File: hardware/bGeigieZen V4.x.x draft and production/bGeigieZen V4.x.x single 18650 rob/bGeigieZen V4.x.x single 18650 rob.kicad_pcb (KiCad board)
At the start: 2 copper layers, 129.4 x 64.6 mm, 13 parts, among them J1 M5 2x15 pin, J2 Geiger IRover, J3 GPS, J4 Geiger Safepulse, J5 Extra support header

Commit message: Added  Assembly manual and Japan Post registered mail numbers.
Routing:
- net /SCL: track 116.3 -> 117.7 mm
- net /GIO2 on Core and GIO32 on Core-2: track 90.4 -> 89.3 mm
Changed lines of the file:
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@@
 	(title_block
 		(title "bGeigieZen Draft V4.0.5 NFW")
-		(date "2024-05-31")
+		(date "2024-06-07")
 		(rev "V4.0.5 rob")
 		(comment 1 "Not For Whimps version.")
@@
 	)
 	(segment
-		(start 149.305 88.3365)
-		(end 129.046 108.595)
-		(width 0.25)
-		(layer "B.Cu")
-		(net 3)
-	)
-	(segment
-		(start 131.679 119.0022)
-		(end 131.679 118.6344)
-		(width 0.25)
-		(layer "B.Cu")
-		(net 3)
-	)
-	(segment
-		(start 131.679 118.6344)
-		(end 130.8701 117.8255)
-		(width 0.25)
-		(layer "B.Cu")
-		(net 3)
-	)
-	(segment
-		(start 132.8557 119.0022)
-		(end 131.679 119.0022)
+		(start 131.679 117.8255)
+		(end 129.9782 117.8255)
 		(width 0.25)
 		(layer "B.Cu")
@@
 	)
 	(segment
-		(start 149.223 88.3365)
-		(end 149.305 88.3365)
+		(start 129.9782 117.8255)
+		(end 129.046 116.8933)
 		(width 0.25)
 		(layer "B.Cu")
@@
 	)
 	(segment
-		(start 130.8701 117.8255)
-		(end 129.9782 117.8255)
+		(start 132.8557 119.0022)
+		(end 131.679 117.8255)
 		(width 0.25)
 		(layer "B.Cu")
@@
 	)
 	(segment
-		(start 129.9782 117.8255)
-		(end 129.046 116.8933)
+		(start 129.046 108.595)
+		(end 149.305 88.3365)
 		(width 0.25)
 		(layer "B.Cu")
@@
 	)
 	(segment
-		(start 188.316 89.7109)
-		(end 188.316 89.7113)
-		(width 0.25)
-		(layer "F.Cu")
-		(net 18)
-	)
-	(segment
-		(start 188.316 89.6082)
-		(end 188.316 89.6086)
+		(start 128.262401 115.2872)
+		(end 128.305401 115.330199)
 		(width 0.25)
 		(layer "F.Cu")
@@
 	)
 	(segment
-		(start 188.316 89.8132)
-		(end 188.316 90.9899)
-		(width 0.25)
-		(layer "F.Cu")
-		(net 18)
-	)
-	(segment
-		(start 184.301 88.3382)
-		(end 187.251 88.3382)
+		(start 197.2056 95.8076)
+		(end 196.003519 95.8076)
 		(width 0.25)
 		(layer "F.Cu")
@@
 	)
 	(segment
-		(start 129.046 113.492)
-		(end 153.436 89.102)
+		(start 188.316 89.8004)
+		(end 188.316 89.8132)
 		(width 0.25)
 		(layer "F.Cu")
@@
 	)
 	(segment
-		(start 153.436 89.102)
-		(end 183.537 89.102)
+		(start 126.6437 116.9919)
+		(end 126.6007 116.948901)
 		(width 0.25)
 		(layer "F.Cu")
@@
 	)
 	(segment
-		(start 129.046 113.492)
-		(end 129.046 116.9229)
+		(start 188.316 89.8004)
+		(end 188.3156 89.8008)
 		(width 0.25)
 		(layer "F.Cu")
@@
 	)
 	(segment
-		(start 187.251 88.3382)
-		(end 188.316 89.4032)
+		(start 188.316 89.6082)
+		(end 188.316 89.6086)
 		(width 0.25)
 		(layer "F.Cu")
@@
 	)
 	(segment
-		(start 188.316 89.8132)
-		(end 188.316 90.9899)
+		(start 190.244634 91.2882)
+		(end 188.756834 89.8004)
 		(width 0.25)
 		(layer "F.Cu")
@@
 	)
 	(segment
-		(start 188.316 89.8004)
-		(end 188.316 89.8132)
+		(start 128.305401 115.330199)
+		(end 155.2974 88.3382)
 		(width 0.25)
 		(layer "F.Cu")
@@
 	)
 	(segment
-		(start 188.316 89.7877)
-		(end 188.316 89.8004)
+		(start 188.316 89.7622)
+		(end 188.316 89.7877)
 		(width 0.25)
 		(layer "F.Cu")
@@
 	(segment
 		(start 188.316 89.4032)
-		(end 188.316 89.6082)
+		(end 188.316 89.8004)
 		(width 0.25)
 		(layer "F.Cu")
@@
 	)
 	(segment
-		(start 183.537 89.102)
-		(end 184.301 88.3382)
+		(start 126.6007 117.0349)
+		(end 126.6437 116.9919)
 		(width 0.25)
 		(layer "F.Cu")
@@
 	)
 	(segment
-		(start 188.316 89.7622)
-		(end 188.316 89.7877)
+		(start 188.316 89.7109)
+		(end 188.316 89.7113)
 		(width 0.25)
 		(layer "F.Cu")
@@
 	)
 	(segment
-		(start 188.316 89.8004)
-		(end 188.316 89.8132)
+		(start 188.316 89.6086)
+		(end 188.316 89.7109)
 		(width 0.25)
 		(layer "F.Cu")
@@
 	(segment
 		(start 127.7757 119.0022)
-		(end 127.7757 117.8255)
+		(end 126.6007 117.8272)
 		(width 0.25)
 		(layer "F.Cu")
@@
 	)
 	(segment
-		(start 188.316 89.8004)
-		(end 188.3156 89.8008)
+		(start 191.484119 91.2882)
+		(end 190.244634 91.2882)
 		(width 0.25)
 		(layer "F.Cu")
@@
 	)
 	(segment
-		(start 188.316 89.6082)
-		(end 188.316 89.6086)
+		(start 188.316 89.7113)
+		(end 188.316 89.7622)
 		(width 0.25)
 		(layer "F.Cu")
@@
 	)
 	(segment
-		(start 188.316 89.6086)
-		(end 188.316 89.7109)
+		(start 188.316 89.7877)
+		(end 188.316 89.8004)
 		(width 0.25)
 		(layer "F.Cu")
@@
 	)
 	(segment
-		(start 129.046 116.9229)
-		(end 128.1434 117.8255)
+		(start 196.003519 95.8076)
+		(end 191.484119 91.2882)
 		(width 0.25)
 		(layer "F.Cu")
@@
 	)
 	(segment
-		(start 193.133 95.8076)
-		(end 188.316 90.9899)
+		(start 188.316 89.8004)
+		(end 188.316 89.8132)
 		(width 0.25)
 		(layer "F.Cu")
@@
 	)
 	(segment
-		(start 188.316 89.7622)
-		(end 188.316 89.7877)
+		(start 126.6007 115.975499)
+		(end 127.288999 115.2872)
 		(width 0.25)
 		(layer "F.Cu")
@@
 	)
 	(segment
-		(start 188.316 89.7113)
-		(end 188.316 89.7622)
+		(start 188.756834 89.8004)
+		(end 188.316 89.8004)
 		(width 0.25)
 		(layer "F.Cu")
@@
 	)
 	(segment
-		(start 188.316 89.6086)
-		(end 188.316 89.7109)
-		(width 0.25)
-		(layer "F.Cu")
-		(net 18)
-	)
-	(segment
-		(start 188.316 89.7113)
-		(end 188.316 89.7622)
-		(width 0.25)
-		(layer "F.Cu")
-		(net 18)
-	)
-	(segment
-		(start 188.316 89.7877)
-		(end 188.316 89.8004)
+		(start 126.6007 116.948901)
+		(end 126.6007 115.975499)
 		(width 0.25)
 		(layer "F.Cu")
@@
 	)
 	(segment
-		(start 128.1434 117.8255)
-		(end 127.7757 117.8255)
+		(start 155.2974 88.3382)
+		(end 187.251 88.3382)
 		(width 0.25)
 		(layer "F.Cu")
@@
 	)
 	(segment
-		(start 188.316 89.8004)
-		(end 188.316 89.8132)
+		(start 188.3156 89.8008)
+		(end 188.3156 89.8132)
 		(width 0.25)
 		(layer "F.Cu")
@@
 	)
 	(segment
-		(start 188.316 89.7109)
-		(end 188.316 89.7113)
+		(start 188.316 89.7622)
+		(end 188.316 89.7877)
 		(width 0.25)
 		(layer "F.Cu")
@@
 	)
 	(segment
-		(start 188.3156 89.8008)
-		(end 188.3156 89.8132)
+		(start 126.6007 117.8272)
+		(end 126.6007 117.0349)
 		(width 0.25)
 		(layer "F.Cu")
@@
 	)
 	(segment
-		(start 188.316 89.7622)
-		(end 188.316 89.7877)
+		(start 187.251 88.3382)
+		(end 188.316 89.4032)
 		(width 0.25)
 		(layer "F.Cu")
@@
 	)
 	(segment
-		(start 197.2056 95.8076)
-		(end 193.133 95.8076)
+		(start 127.288999 115.2872)
+		(end 128.262401 115.2872)
 		(width 0.25)
 		(layer "F.Cu")
@@
 	)
 	(segment
-		(start 130.3157 117.8255)
-		(end 130.3157 119.0022)
+		(start 130.3157 119.0022)
+		(end 131.572 117.7459)
 		(width 0.25)
 		(layer "F.Cu")
@@
 	)
 	(segment
-		(start 131.5857 114.5383)
-		(end 144.856 101.269)
+		(start 196.594634 99.8226)
+		(end 195.1736 98.401566)
 		(width 0.25)
 		(layer "F.Cu")
@@
 	)
 	(segment
-		(start 155.854 90.2704)
-		(end 144.856 101.269)
+		(start 199.291783 94.381817)
+		(end 199.291783 98.347383)
 		(width 0.25)
 		(layer "F.Cu")
@@
 	)
 	(segment
-		(start 198.681 97.7366)
-		(end 198.681 98.9586)
+		(start 155.9054 90.2196)
+		(end 144.856 101.269)
 		(width 0.25)
 		(layer "F.Cu")
@@
 	)
 	(segment
-		(start 131.5857 114.5383)
-		(end 131.572 114.552)
-		(width 0.25)
-		(layer "F.Cu")
-		(net 25)
-	)
-	(segment
-		(start 192.835 99.8226)
-		(end 183.283 90.2704)
+		(start 191.413966 98.401566)
+		(end 183.232 90.2196)
 		(width 0.25)
 		(layer "F.Cu")
@@
 	)
 	(segment
-		(start 209.155 91.9718)
-		(end 209.1551 91.9718)
+		(start 131.572 114.552)
+		(end 131.5857 114.5383)
 		(width 0.25)
 		(layer "F.Cu")
@@
 	)
 	(segment
-		(start 131.572 114.552)
-		(end 131.572 116.8735)
+		(start 195.1736 98.401566)
+		(end 191.413966 98.401566)
 		(width 0.25)
 		(layer "F.Cu")
@@
 	)
 	(segment
-		(start 183.283 90.2704)
-		(end 155.854 90.2704)
+		(start 209.1551 91.9718)
+		(end 201.7018 91.9718)
 		(width 0.25)
 		(layer "F.Cu")
@@
 	)
 	(segment
-		(start 204.445 91.9718)
-		(end 198.681 97.7366)
+		(start 199.291783 98.347383)
+		(end 197.816566 99.8226)
 		(width 0.25)
 		(layer "F.Cu")
@@
 	)
 	(segment
-		(start 130.62 117.8255)
-		(end 130.3157 117.8255)
+		(start 201.7018 91.9718)
+		(end 199.291783 94.381817)
 		(width 0.25)
 		(layer "F.Cu")
@@
 	)
 	(segment
-		(start 131.572 116.8735)
-		(end 130.62 117.8255)
+		(start 183.232 90.2196)
+		(end 155.9054 90.2196)
 		(width 0.25)
 		(layer "F.Cu")
@@
 	)
 	(segment
-		(start 198.681 98.9586)
-		(end 197.817 99.8226)
+		(start 197.816566 99.8226)
+		(end 196.594634 99.8226)
 		(width 0.25)
 		(layer "F.Cu")
@@
 	)
 	(segment
-		(start 197.817 99.8226)
-		(end 192.835 99.8226)
+		(start 131.5857 114.5383)
+		(end 144.856 101.269)
 		(width 0.25)
 		(layer "F.Cu")
@@
 	)
 	(segment
-		(start 209.155 91.9718)
-		(end 204.445 91.9718)
+		(start 131.572 117.7459)
+		(end 131.572 114.552)
 		(width 0.25)
 		(layer "F.Cu")

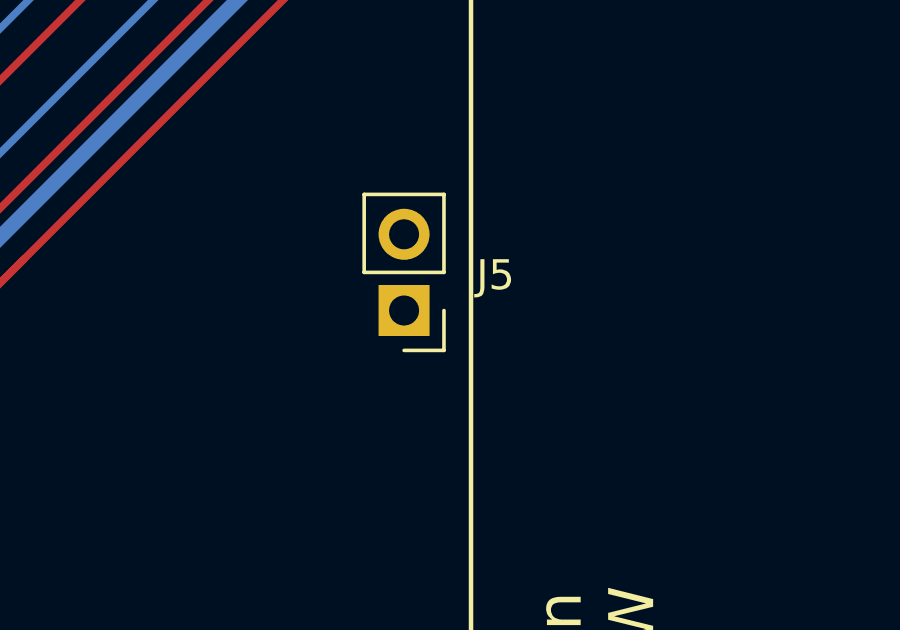
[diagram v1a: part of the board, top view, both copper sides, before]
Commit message: Updated  pin header placement of safepulse
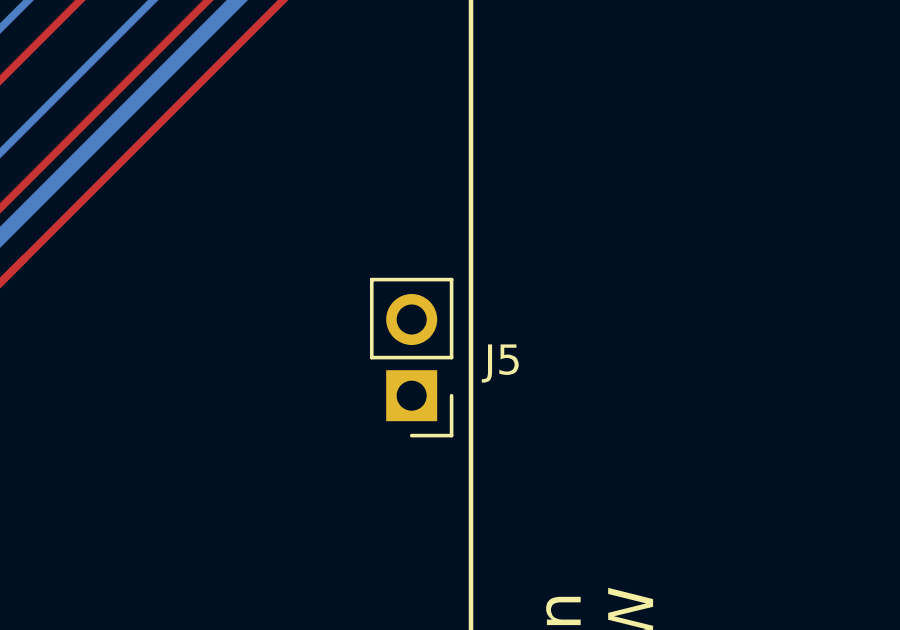
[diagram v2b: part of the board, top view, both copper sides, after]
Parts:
- moved J5 2.85 mm to (157.8, 105.8)
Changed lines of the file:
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@@
 	(footprint "Connector_PinHeader_2.54mm:PinHeader_1x02_P2.54mm_Vertical"
 		(layer "F.Cu")
-		(at 157.5308 102.9754 180)
+		(at 157.7848 105.8152 180)
 		(descr "Through hole straight pin header, 1x02, 2.54mm pitch, single row")
 		(tags "Through hole pin header THT 1x02 2.54mm single row")
@@
 	)
 	(gr_line
-		(start 153.6446 103.4088)
-		(end 153.6446 90.086)
+		(start 153.6192 104.4408)
+		(end 153.6192 90.7812)
 		(stroke
-			(width 0.12)
+			(width 0.2)
 			(type default)
 		)
@@
 	)
 	(gr_arc
-		(start 155.6446 105.4088)
-		(mid 154.230386 104.823014)
-		(end 153.6446 103.4088)
+		(start 191.7672 87.7812)
+		(mid 193.88852 88.65988)
+		(end 194.7672 90.7812)
 		(stroke
-			(width 0.12)
+			(width 0.2)
 			(type default)
 		)
@@
 	)
 	(gr_arc
-		(start 194.2338 103.4088)
-		(mid 193.648014 104.823014)
-		(end 192.2338 105.4088)
+		(start 194.7672 104.4408)
+		(mid 193.88852 106.56212)
+		(end 191.7672 107.4408)
 		(stroke
-			(width 0.12)
+			(width 0.2)
 			(type default)
 		)
@@
 	)
 	(gr_arc
-		(start 153.6446 90.086)
-		(mid 154.230386 88.671786)
-		(end 155.6446 88.086)
+		(start 156.6192 107.4408)
+		(mid 154.49788 106.56212)
+		(end 153.6192 104.4408)
 		(stroke
-			(width 0.12)
+			(width 0.2)
 			(type default)
 		)
@@
 	)
 	(gr_line
-		(start 194.2338 90.086)
-		(end 194.2338 103.4088)
+		(start 194.7672 90.7812)
+		(end 194.7672 104.4408)
 		(stroke
-			(width 0.12)
+			(width 0.2)
 			(type default)
 		)
@@
 	)
 	(gr_line
-		(start 155.6446 88.086)
-		(end 192.2338 88.086)
+		(start 191.7672 107.4408)
+		(end 156.6192 107.4408)
 		(stroke
-			(width 0.12)
+			(width 0.2)
 			(type default)
 		)
 		(layer "B.SilkS")
 	)
-	(gr_arc
-		(start 192.2338 88.086)
-		(mid 193.648014 88.671786)
-		(end 194.2338 90.086)
+	(gr_line
+		(start 156.6192 87.7812)
+		(end 191.7672 87.7812)
 		(stroke
-			(width 0.12)
+			(width 0.2)
 			(type default)
 		)
 		(layer "B.SilkS")
 	)
-	(gr_line
-		(start 192.2338 105.4088)
-		(end 155.6446 105.4088)
+	(gr_arc
+		(start 153.6192 90.7812)
+		(mid 154.49788 88.65988)
+		(end 156.6192 87.7812)
 		(stroke
-			(width 0.12)
+			(width 0.2)
 			(type default)
 		)
@@
 		(layer "Edge.Cuts")
 	)
-	(gr_text "Safepulse"
-		(at 177.3428 89.864 0)
+	(gr_text "bGeigieZen\nV4.0.5 NFW"
+		(at 200.5584 112.724 90)
 		(layer "B.SilkS")
 		(effects
@@
 				(size 1.5 1.5)
 				(thickness 0.3)
-				(bold yes)
 			)
-			(justify mirror)
+			(justify left mirror)
 		)
 	)
-	(gr_text "bGeigieZen\nV4.0.5 NFW"
-		(at 200.5584 112.724 90)
+	(gr_text "Irover"
+		(at 197.3072 103.58 90)
 		(layer "B.SilkS")
 		(effects
@@
 				(size 1.5 1.5)
 				(thickness 0.3)
+				(bold yes)
 			)
-			(justify left mirror)
+			(justify mirror)
 		)
 	)
-	(gr_text "Irover"
-		(at 197.3072 103.58 90)
+	(gr_text "Safepulse"
+		(at 176.3268 89.9148 0)
 		(layer "B.SilkS")
 		(effects
@@
 	)
 	(group ""
-		(members "2e1e894e-7567-4071-a668-46d6ebfb9665" "35e36128-6801-4c0a-8941-083c7e89a3d8"
-			"5f05a722-553c-4d30-8de3-d6298ff2b16e" "693bfb3e-6025-4ee9-a4ed-ac25da7d9da5"
-			"734542f1-9af4-4a1a-a0aa-203a1626f31a" "8103ad81-a648-46c1-a7d5-c4b623ea342d"
-			"9ce7780d-eb87-463c-be14-50af85c17fdc" "aef80be5-6fb2-4a43-9f41-e8b5022bdc8e"
-			"e1a0cc2e-1057-4757-8a17-f759adb29c4b"
+		(members "16589174-4883-488a-a310-3bf6c969f2e0" "1a3b2ad6-e32d-4da1-8853-b6ab0127027c"
+			"238354a2-e4f2-449c-8ff5-80816443489e" "26ff2ced-6396-4ded-a81f-8680827d846b"
+			"49ac0fb7-d048-42be-819d-be7a804dd479" "90b63bb7-2192-4388-a59e-9fe57a81764a"
+			"b1d42241-f50c-4ca7-b9c9-0c58e1577583" "e82afe44-bb57-445e-981a-a6ab6f09c393"
+			"fd799f7b-5ed7-4f63-901a-f4dc64e1af37"
 		)
 	)

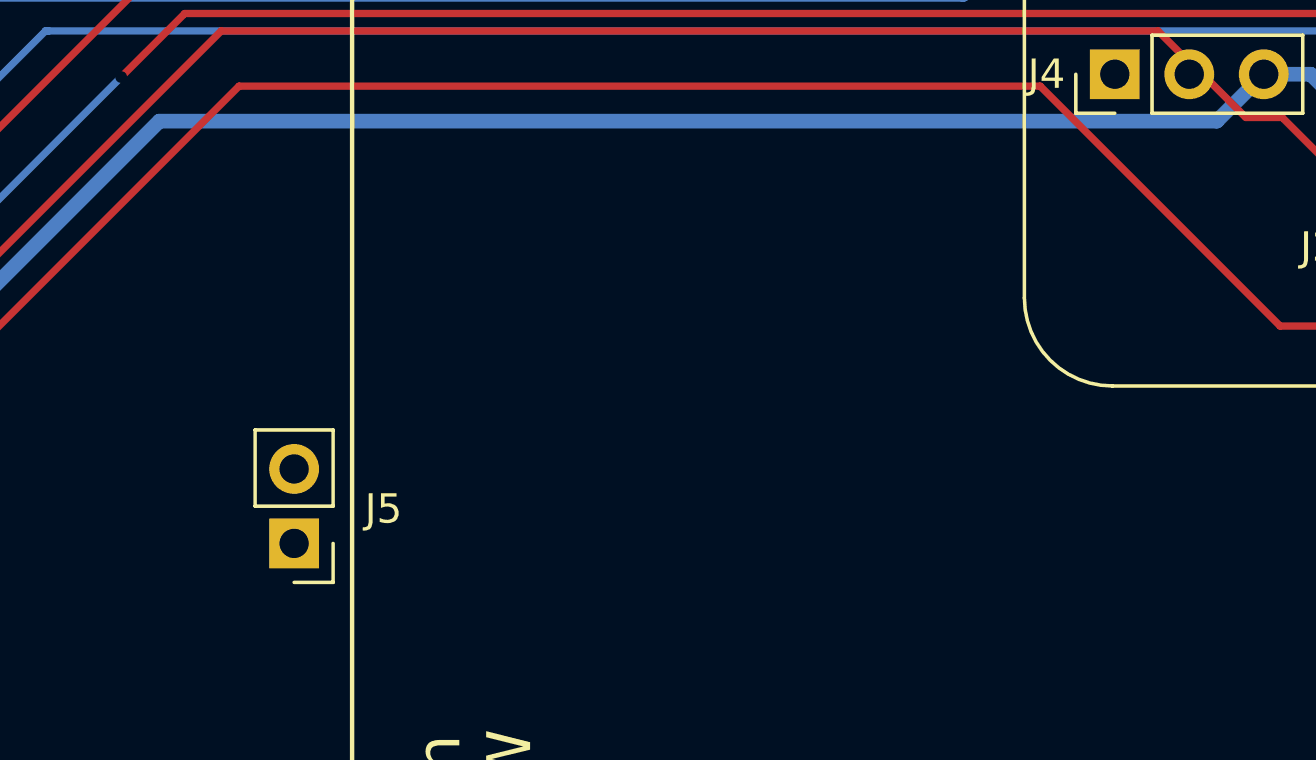
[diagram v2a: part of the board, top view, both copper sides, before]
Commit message: Updated footprints for the Safepulse on 4.x.x boards
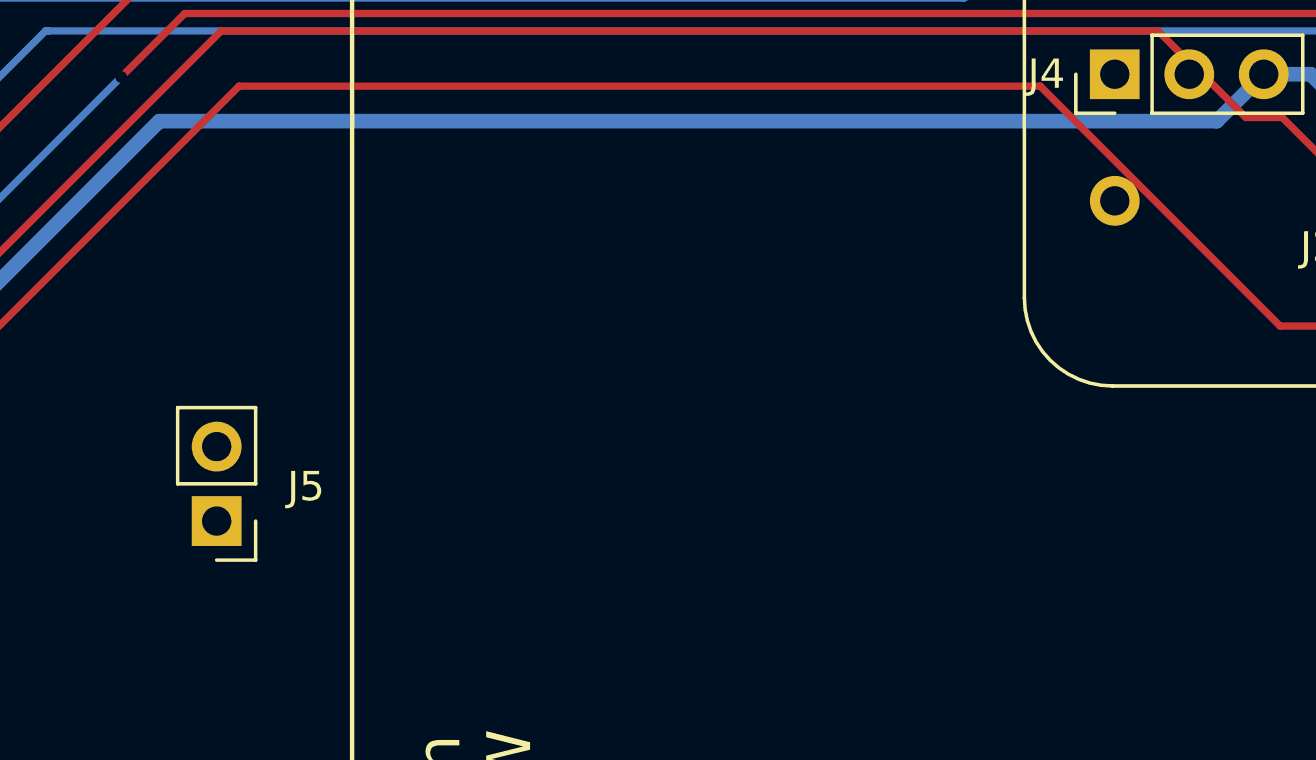
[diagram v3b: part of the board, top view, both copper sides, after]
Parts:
- added ?: , , F.Cu at (185.8, 94.1)
- moved J5 2.75 mm to (155.1, 105.1)
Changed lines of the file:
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@@
 	(footprint "Connector_PinHeader_2.54mm:PinHeader_1x02_P2.54mm_Vertical"
 		(layer "F.Cu")
-		(at 157.7848 105.8152 180)
+		(at 155.1432 105.0532 180)
 		(descr "Through hole straight pin header, 1x02, 2.54mm pitch, single row")
 		(tags "Through hole pin header THT 1x02 2.54mm single row")
@@
 		)
 	)
+	(footprint ""
+		(layer "F.Cu")
+		(at 185.7756 94.1312 180)
+		(property "Reference" ""
+			(at 0 0 360)
+			(layer "F.SilkS")
+			(effects
+				(font
+					(size 1.27 1.27)
+					(thickness 0.15)
+				)
+			)
+		)
+		(property "Value" ""
+			(at 0 0 360)
+			(layer "F.Fab")
+			(effects
+				(font
+					(size 1.27 1.27)
+					(thickness 0.15)
+				)
+			)
+		)
+		(property "Footprint" ""
+			(at 0 0 360)
+			(layer "F.Fab")
+			(hide yes)
+			(effects
+				(font
+					(size 1.27 1.27)
+					(thickness 0.15)
+				)
+			)
+		)
+		(property "Datasheet" ""
+			(at 0 0 360)
+			(layer "F.Fab")
+			(hide yes)
+			(effects
+				(font
+					(size 1.27 1.27)
+					(thickness 0.15)
+				)
+			)
+		)
+		(property "Description" ""
+			(at 0 0 360)
+			(layer "F.Fab")
+			(hide yes)
+			(effects
+				(font
+					(size 1.27 1.27)
+					(thickness 0.15)
+				)
+			)
+		)
+		(pad "3" thru_hole oval
+			(at 0 0 270)
+			(size 1.7 1.7)
+			(drill 1)
+			(layers "*.Cu" "*.Mask")
+			(remove_unused_layers no)
+			(net 1 "GND")
+			(pinfunction "Pin_3")
+			(pintype "passive")
+		)
+	)
 	(footprint "MountingHole:MountingHole_3.2mm_M3"
 		(layer "F.Cu")
@@
 	)
 	(gr_line
-		(start 153.6192 104.4408)
-		(end 153.6192 90.7812)
+		(start 152.9588 104.6186)
+		(end 152.9588 90.959)
 		(stroke
 			(width 0.2)
@@
 	)
 	(gr_arc
-		(start 191.7672 87.7812)
-		(mid 193.88852 88.65988)
-		(end 194.7672 90.7812)
+		(start 191.1068 87.959)
+		(mid 193.22812 88.83768)
+		(end 194.1068 90.959)
 		(stroke
 			(width 0.2)
@@
 	)
 	(gr_arc
-		(start 194.7672 104.4408)
-		(mid 193.88852 106.56212)
-		(end 191.7672 107.4408)
+		(start 194.1068 104.6186)
+		(mid 193.22812 106.73992)
+		(end 191.1068 107.6186)
 		(stroke
 			(width 0.2)
@@
 	)
 	(gr_arc
-		(start 156.6192 107.4408)
-		(mid 154.49788 106.56212)
-		(end 153.6192 104.4408)
+		(start 155.9588 107.6186)
+		(mid 153.83748 106.73992)
+		(end 152.9588 104.6186)
 		(stroke
 			(width 0.2)
@@
 	)
 	(gr_line
-		(start 194.7672 90.7812)
-		(end 194.7672 104.4408)
+		(start 194.1068 90.959)
+		(end 194.1068 104.6186)
 		(stroke
 			(width 0.2)
@@
 	)
 	(gr_line
-		(start 191.7672 107.4408)
-		(end 156.6192 107.4408)
+		(start 191.1068 107.6186)
+		(end 155.9588 107.6186)
 		(stroke
 			(width 0.2)
@@
 	)
 	(gr_line
-		(start 156.6192 87.7812)
-		(end 191.7672 87.7812)
+		(start 155.9588 87.959)
+		(end 191.1068 87.959)
 		(stroke
 			(width 0.2)
@@
 	)
 	(gr_arc
-		(start 153.6192 90.7812)
-		(mid 154.49788 88.65988)
-		(end 156.6192 87.7812)
+		(start 152.9588 90.959)
+		(mid 153.83748 88.83768)
+		(end 155.9588 87.959)
 		(stroke
 			(width 0.2)
@@
 	)
 	(gr_text "Safepulse"
-		(at 176.3268 89.9148 0)
+		(at 175.6664 90.0926 0)
 		(layer "B.SilkS")
 		(effects
